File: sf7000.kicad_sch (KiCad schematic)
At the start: 114 parts

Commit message: labeled IC33
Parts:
- C1: value (none) -> 100u
- C10, C11, C18, C19, C20, C21, C22, C4, C43, C44, C5, C6, C7, C8, C9, C?: value (none) -> 100n
- C12, C13, C?: value (none) -> 33p
- C14: value (none) -> 470p
- C15, C16, C23: value (none) -> C
- C2, C38: value (none) -> 22p
- C34, C45: value (none) -> CP
- C35, C36: value (none) -> 10u
- C40, C41, C42: value (none) -> 220p
- CN1: value (none) -> Conn_01x03_Female
- CN2-A: value (none) -> Floppy_34pin
- CN2-B: value (none) -> Floppy_26pin
- CN3, CN?: value (none) -> Conn_02x17_Odd_Even
- CN4: value (none) -> Centronics 14 pin
- CN5: value (none) -> DB25_Female
- D1, D2, D7, D8: value (none) -> 1S1588
- D9: value (none) -> D_Zener
- DSW1: value (none) -> SW_DIP_x06
- IC10?, IC11?, IC12?, IC5, IC6, IC7, IC8, IC9?: value (none) -> MB8264
- IC13: value (none) -> M5L2764K
- IC14, IC21: value (none) -> 74LS00
- IC15: value (none) -> 74LS02
- IC16, IC17, IC37: value (none) -> 74LS04
- IC18: value (none) -> 74LS06
- IC19: value (none) -> 74LS07
- IC20: value (none) -> 74LS14
- IC22: value (none) -> 74LS139
- IC23, IC24, IC25: value (none) -> 74LS157
- IC26: value (none) -> 74LS32
- IC27, IC28: value (none) -> 74LS244
- IC3: value (none) -> uPD765A
- IC30: value (none) -> 74LS367
- IC33: renamed from U?; value (none) -> 8255A; footprint (none) -> Package_DIP:DIP-40_W15.24mm
- IC33: value (none) -> 8251
- IC34: value (none) -> SN75188
- IC35: value (none) -> SN75189
- IC36: value (none) -> 74LS293
- IC38: value (none) -> 4040
- IC4: value (none) -> SED9420C
- J?: value (none) -> JP_Overlay
- JP? (x2): value (none) -> SolderJumper_2_Open
- L?: value (none) -> L
- LED1: value (none) -> RD
- LED2: value (none) -> SD
- LED3: value (none) -> LED
- Q?: value (none) -> Q_PNP_ECB
- R1: value (none) -> 2K2
- R10: value (none) -> 1M
- R11, R14, R15, R4: value (none) -> 470
- R13: value (none) -> 220
- R16, R6: value (none) -> 10K
- R17: value (none) -> 18K
- R18, R19, RA1(1/8): value (none) -> 4k7
- R2, R7: value (none) -> 22K
- R20: value (none) -> 47K
- R3: value (none) -> 3K3
- R5: value (none) -> 4.7K
- R8: value (none) -> 150K
- R9: value (none) -> 560K
- RA1: value (none) -> K; footprint (none) -> Resistor_THT:R_Array_SIP9
- RA2: value (none) -> 1K; footprint (none) -> Resistor_THT:R_Array_SIP7
- RN?: value (none) -> R_Network08; footprint (none) -> Resistor_THT:R_Array_SIP9
- TR3: value (none) -> Q_NPN_ECB
- XAL2: value (none) -> 4.9152MHz
- XR1: value (none) -> 16Mhz

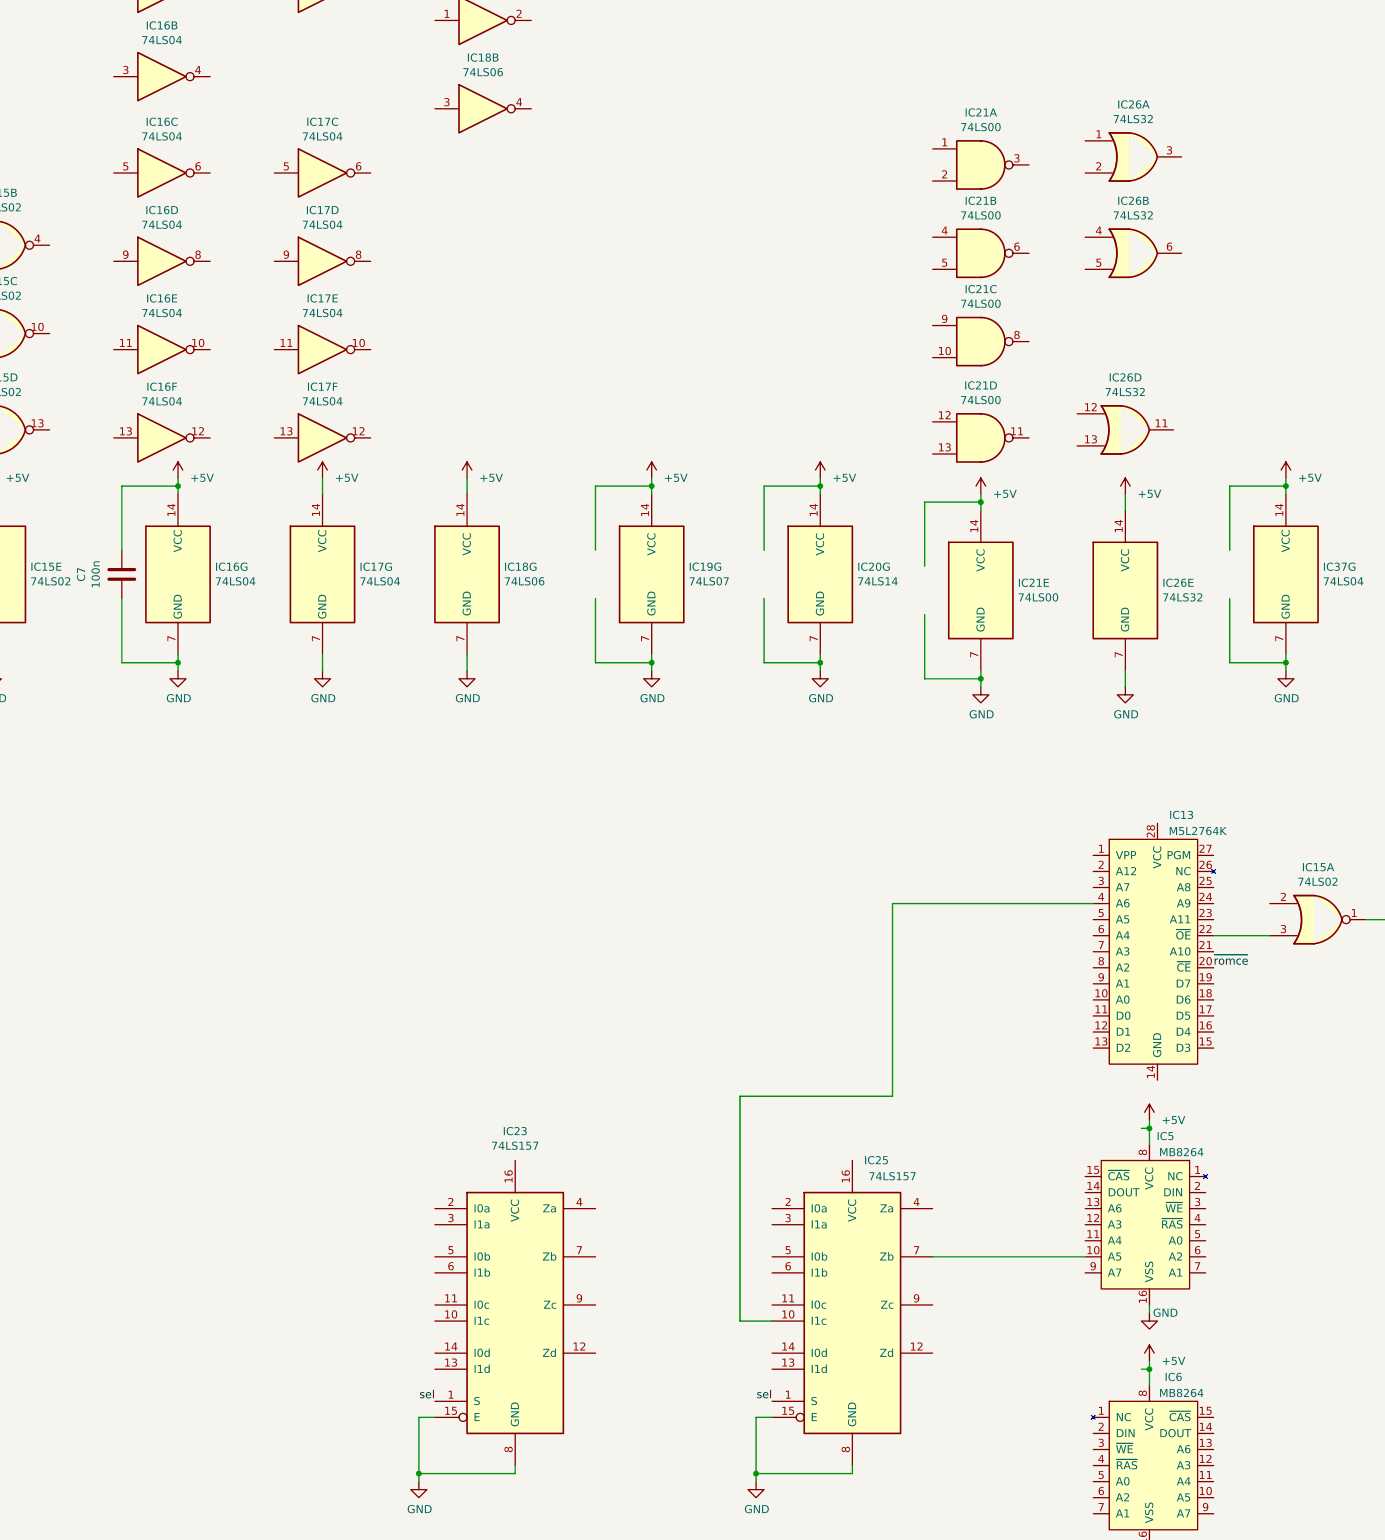
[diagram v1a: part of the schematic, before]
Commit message: IC25, info from andrea applied
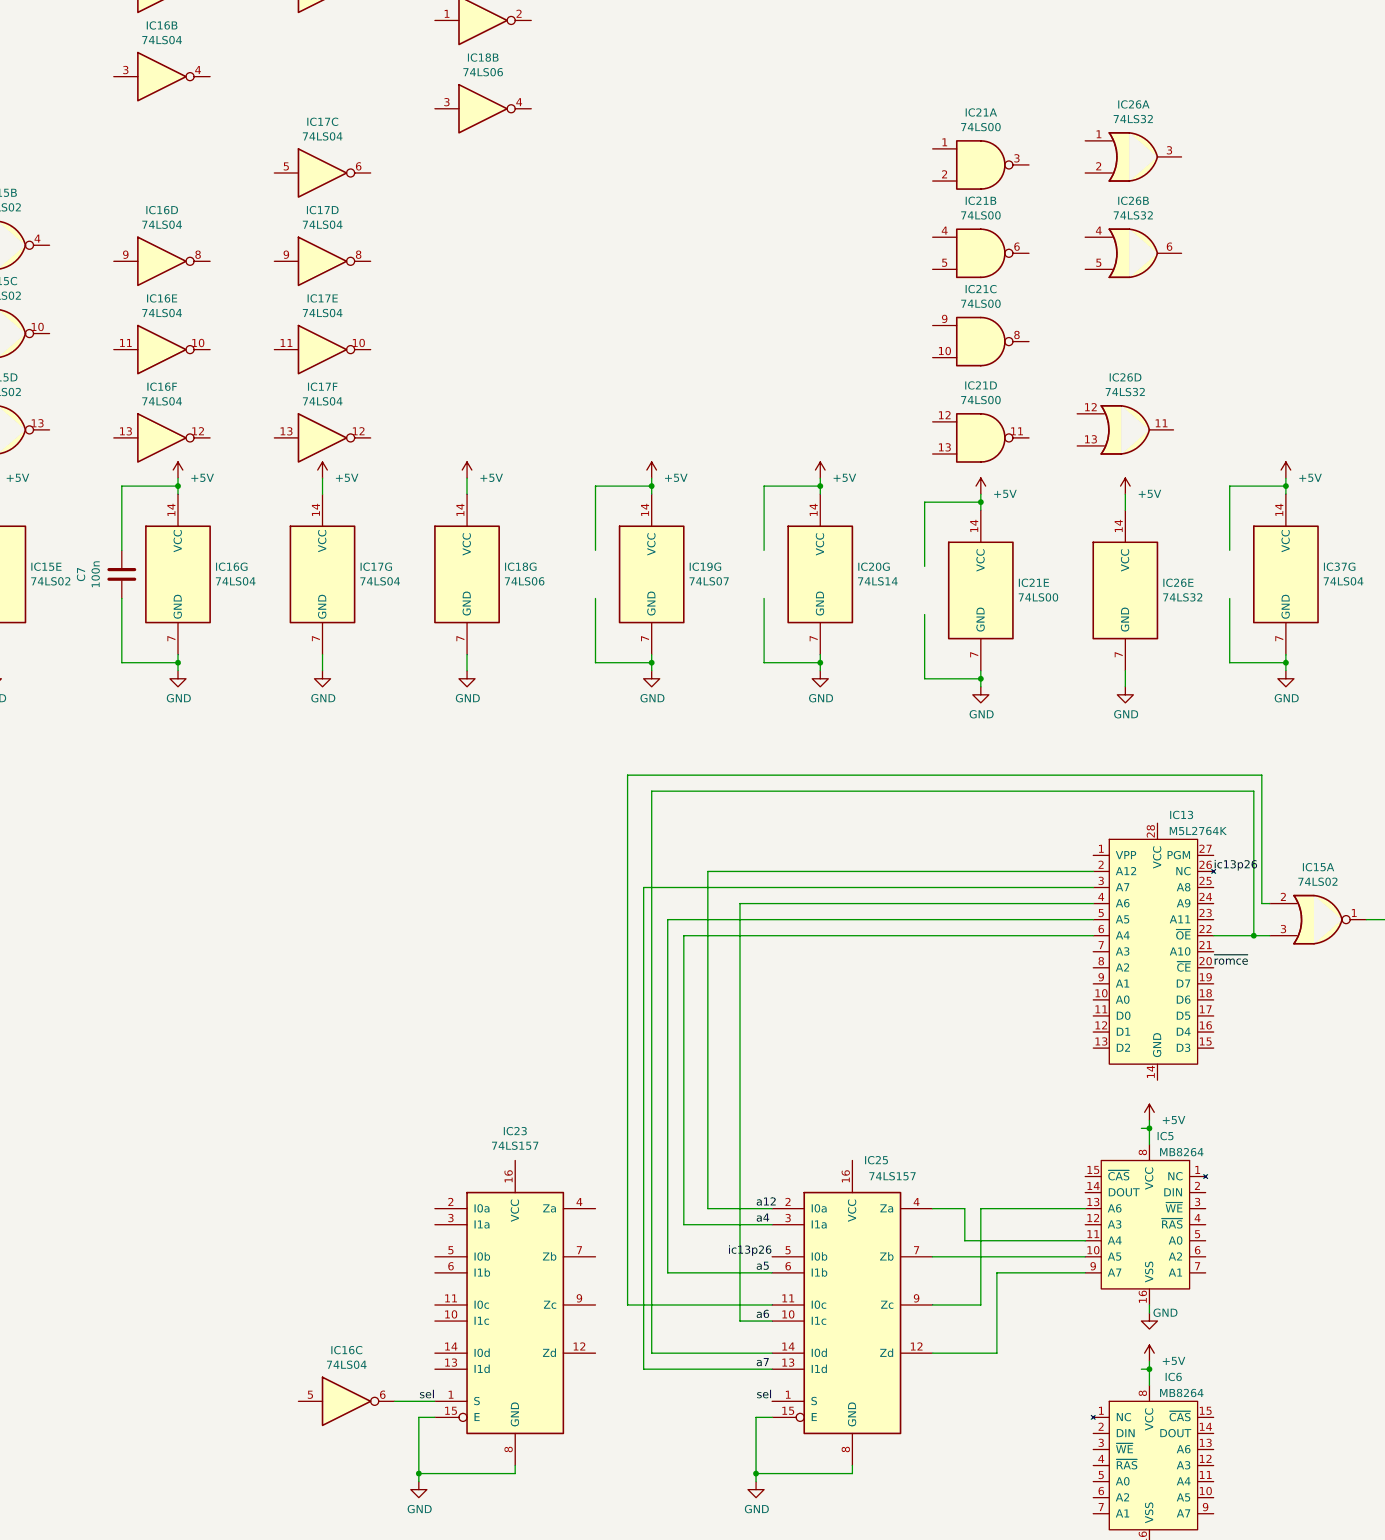
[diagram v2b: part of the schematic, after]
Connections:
- net a12: now also IC13.2 (A12), IC25.2 (I0a)
- net a4: now also IC13.6 (A4), IC25.3 (I1a)
- net a5: now also IC13.5 (A5), IC25.6 (I1b)
- net a6: now also IC13.4 (A6), IC25.10 (I1c)
- net a7: now also IC13.3 (A7), IC25.13 (I1d)
- net sel: now also IC16.6
- net at IC25.11 (I0c): now also IC15.2
- net at IC25.12 (Zd): now also IC5.9 (A7)
- net at IC25.14 (I0d): now also IC13.22 (~{OE}), IC15.3
- net at IC25.4 (Za): now also IC5.11 (A4)
- net ic13p26: now reaches IC25.5 (I0b)
- net ic13p26: now also IC13.26 (NC)
- net at IC25.9 (Zc): now also IC5.13 (A6)
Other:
- moved on the sheet: IC16C

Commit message: symbol for polarized cap
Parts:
- C1, C34, C35, C36, C45: symbol Device:CP -> Device:C_Polarized
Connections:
- net +5V: now also C1.1, C45.1
- net -12V: now also C35.2
- net GND: now also C1.2, C35.1, C36.2, C45.2
- net at C?.1, L?.2, TR3.2 (C): now also C34.1
- net at D1.1 (K), D2.2 (A): now also C34.2
- net at D7.2 (A), IC20.1, R6.2: now also C36.1
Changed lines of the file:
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@@
     (pin "7")
   )
-  (symbol (lib_id "Device:CP") (at 396.24 26.67 270) (unit 1)
+  (symbol (lib_id "Device:C_Polarized") (at 396.24 26.67 270) (unit 1)
     (in_bom yes) (on_board yes)
     (property "Reference" "C45" (id 0) (at 396.24 20.193 90))
@@
       (effects (font (size 1.27 1.27)) hide)
     )
+    (pin "1")
+    (pin "2")
   )
   (symbol (lib_id "power:GND") (at 391.16 26.67 270) (unit 1)
@@
     (pin "7")
   )
-  (symbol (lib_id "Device:CP") (at 97.79 152.4 90) (unit 1)
+  (symbol (lib_id "Device:C_Polarized") (at 97.79 152.4 90) (unit 1)
     (in_bom yes) (on_board yes)
     (property "Reference" "C34" (id 0) (at 97.79 156.21 90))
@@
       (effects (font (size 1.27 1.27)) hide)
     )
+    (pin "1")
+    (pin "2")
   )
   (symbol (lib_id "74xx:74LS00") (at 251.46 349.25 0) (unit 1)
@@
     (pin "7")
   )
-  (symbol (lib_id "Device:CP") (at 113.03 176.53 90) (unit 1)
+  (symbol (lib_id "Device:C_Polarized") (at 113.03 176.53 90) (unit 1)
     (in_bom yes) (on_board yes)
     (property "Reference" "C35" (id 0) (at 113.03 180.34 90))
@@
       (effects (font (size 1.27 1.27)) hide)
     )
+    (pin "1")
+    (pin "2")
   )
   (symbol (lib_id "Device:D_Zener") (at 113.03 168.91 0) (unit 1)
@@
     (pin "2")
   )
-  (symbol (lib_id "Device:CP") (at 33.02 209.55 0) (unit 1)
+  (symbol (lib_id "Device:C_Polarized") (at 33.02 209.55 0) (unit 1)
     (in_bom yes) (on_board yes)
     (property "Reference" "C36" (id 0) (at 26.543 209.55 90))
@@
       (effects (font (size 1.27 1.27)) hide)
     )
+    (pin "1")
+    (pin "2")
   )
   (symbol (lib_id "power:+5V") (at 33.02 193.04 0) (unit 1)
@@
     (pin "2")
   )
-  (symbol (lib_id "Device:CP") (at 45.72 148.59 0) (unit 1)
+  (symbol (lib_id "Device:C_Polarized") (at 45.72 148.59 0) (unit 1)
     (in_bom yes) (on_board yes)
     (property "Reference" "C1" (id 0) (at 39.243 148.59 90))
@@
       (effects (font (size 1.27 1.27)) hide)
     )
+    (pin "1")
+    (pin "2")
   )
   (symbol (lib_id "Connector:Conn_01x03_Female") (at 19.05 144.78 180) (unit 1)

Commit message: traced address decoding logic
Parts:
- removed C?: 33p, symbol Device:C
- removed RA1(1/8): 4k7, symbol Device:R
- added C24, C25, C26, C27, C37, C39: 100n, symbol Device:C
- added C_back1: 390p, symbol Device:C
- C1: value 100u -> 100uF 16v
- C15: value C -> 1nF
- RA1: value K -> 4K7
- gave numbers to parts that had none: 12
- renumbered CN2-A to CN2-A1, CN2-B to CN2-B1, IC33 to IC2
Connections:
- net 8355CS is gone; now on net 8255CS: IC22.5 (O1)
- net ic13p26 is gone; now on net a13: IC13.26 (NC), IC25.5 (I0b)
- net idcint is gone; now on net fdcint: IC4.5 (DRQ)
- net in_use is gone; now on an unnamed net: IC19.9
- net mot_on is gone; now on an unnamed net: IC19.13
- net ready is gone; now on net PPI_Ready: JP2.2 (B)
- net rstct is gone; now on net RESET: IC26.10
- net +5V: now also C10.2, C15.2, C18.2, C19.2, C20.2, C21.2, C22.2, C5.2, IC13.1 (VPP), IC13.27 (PGM), IC13.28 (VCC), IC23.16 (VCC), IC24.16 (VCC), IC25.16 (VCC), IC28.20 (VCC), R18.2, R19.2, RA1.1 (R1.1), C24.2, C25.2, C26.2, C27.2, C37.2, C39.2, C_back1.1; no longer C1.1
- net GND: now also C10.1, C15.1, C18.1, C19.1, C20.1, C21.1, C22.1, C5.1, IC13.14 (GND), IC33.4 (GND), R1.1, C24.1, C25.1, C26.1, C27.1, C37.1, C39.1; no longer C1.2
- net a0: now also IC13.10 (A0), IC2.9 (A0), IC23.3 (I1a), IC33.12 (C/D)
- net a1: now also IC13.9 (A1), IC2.8 (A1), IC23.6 (I1b)
- net a10: now also IC13.21 (A10), IC23.11 (I0c)
- net a11: now also IC13.23 (A11), IC23.14 (I0d)
- net a14: now also IC15.2, IC25.11 (I0c)
- net a15: now also IC15.3, IC25.14 (I0d)
- net a2: now also IC13.8 (A2), IC23.10 (I1c)
- net a3: now also IC13.7 (A3), IC23.13 (I1d)
- net a8: now also IC13.25 (A8), IC23.2 (I0a)
- net a9: now also IC13.24 (A9), IC23.5 (I0b)
- net d0: now also IC13.11 (D0), IC5.14 (DOUT), IC5.2 (DIN)
- net d1: now also IC13.12 (D1), IC6.14 (DOUT), IC6.2 (DIN)
- net d2: now also IC13.13 (D2), IC7.2 (DIN)
- net d3: now also IC13.15 (D3), IC8.14 (DOUT), IC8.2 (DIN)
- net d4: now also IC13.16 (D4), IC9.2 (DIN)
- net d5: now also IC10.2 (DIN), IC13.17 (D5)
- net d6: now also IC11.2 (DIN), IC13.18 (D6)
- net d7: now also IC12.2 (DIN), IC13.19 (D7)
- net fdcint: now also IC2.4 (PA0)
- net index: now also CN2-A1.8 (~{INDEX}), CN2-B1.2 (INDEX), IC20.13, RA2.2 (R1.2); no longer IC20.12, IC3.17 (IDX)
- net pbusy: now also IC2.3 (PA1), RA1.3 (R2.2)
- net pd0: now also IC2.18 (PB0)
- net pd1: now also IC2.19 (PB1)
- net pd2: now also IC2.20 (PB2)
- net pd3: now also IC2.21 (PB3)
- net pd4: now also IC2.22 (PB4)
- net pd5: now also IC2.23 (PB5)
- net pd6: now also IC2.24 (PB6)
- net pd7: now also IC2.25 (PB7)
- net reset55: now also IC2.35 (RESET)
- net tc: now also IC2.16 (PC2), RA1.7 (R6.2)
- net ~{ior}: now also IC21.13, R19.1
- net ~{iow}: now also IC21.1, R18.1
- net ~{memr}: now also IC21.12, IC26.5
- net ~{memw}: now also IC21.2, IC26.2
- net ~{mreq}: now also IC16.13
- net ~{pstb}: now also IC2.10 (PC7), RA1.4 (R3.2)
- net ~{romce}: now also IC14.1, IC17.4
- net at IC3.15 (~{DACK}): now also RA1.2 (R1.2)
- net A7_Ram: now reaches IC25.12 (Zd), IC5.9 (A7)
- net A7_Ram: now also IC10.9 (A7), IC11.9 (A7), IC12.9 (A7), IC6.9 (A7), IC7.9 (A7), IC8.9 (A7), IC9.9 (A7)
- net A4_Ram: now reaches IC25.4 (Za), IC5.11 (A4)
- net A4_Ram: now also IC10.11 (A4), IC11.11 (A4), IC12.11 (A4), IC6.11 (A4), IC7.11 (A4), IC8.11 (A4), IC9.11 (A4)
- net A5_Ram: now reaches IC25.7 (Zb), IC5.10 (A5)
- net A5_Ram: now also IC10.10 (A5), IC11.10 (A5), IC12.10 (A5), IC6.10 (A5), IC7.10 (A5), IC8.10 (A5), IC9.10 (A5)
- net A6_Ram: now reaches IC25.9 (Zc), IC5.13 (A6)
- net A6_Ram: now also IC10.13 (A6), IC11.13 (A6), IC12.13 (A6), IC6.13 (A6), IC7.13 (A6), IC8.13 (A6), IC9.13 (A6)
- net ~{ROMSEL}: now reaches IC2.11 (PC6)
- net ~{ROMSEL}: now also IC15.11, R1.2
- net PPI_Ready: now reaches IC2.12 (PC5)
- net at IC2.14 (PC0): now also RA1.9 (R8.2)
- net at IC2.15 (PC1): now also RA1.8 (R7.2)
- net RESET: now reaches IC2.17 (PC3)
- net RESET: now also RA1.6 (R5.2)
- net ~{PPI_WR}: now reaches IC2.36 (~{WR})
- net ~{PPI_WR}: now also IC21.6
- net ~{PPI_RD}: now reaches IC2.5 (~{RD})
- net ~{PPI_RD}: now also IC21.8
- net 8255CS: now reaches IC2.6 (~{CS})
- net at IC14.2: now also IC15.13, IC16.9
- net at IC14.3: now also IC14.4
- net A3_Ram: now reaches IC5.12 (A3)
- net A3_Ram: now also IC10.12 (A3), IC11.12 (A3), IC12.12 (A3), IC23.12 (Zd), IC6.12 (A3), IC7.12 (A3), IC8.12 (A3), IC9.12 (A3)
- net ~{CAS}: now reaches IC5.15 (~{CAS})
- net ~{CAS}: now also IC10.15 (~{CAS}), IC11.15 (~{CAS}), IC12.15 (~{CAS}), IC17.2, IC6.15 (~{CAS}), IC7.15 (~{CAS}), IC8.15 (~{CAS}), IC9.15 (~{CAS})
- net WE_Ram: now reaches IC5.3 (~{WE})
- net WE_Ram: now also IC10.3 (~{WE}), IC11.3 (~{WE}), IC12.3 (~{WE}), IC14.13, IC26.3, IC6.3 (~{WE}), IC7.3 (~{WE}), IC8.3 (~{WE}), IC9.3 (~{WE})
- net ~{RAS}: now reaches IC5.4 (~{RAS})
- net ~{RAS}: now also IC10.4 (~{RAS}), IC11.4 (~{RAS}), IC12.4 (~{RAS}), IC16.10, IC21.10, IC21.5, IC26.1, IC26.4, IC6.4 (~{RAS}), IC7.4 (~{RAS}), IC8.4 (~{RAS}), IC9.4 (~{RAS}), C_back1.2
- net A0_Ram: now reaches IC5.5 (A0)
- net A0_Ram: now also IC10.5 (A0), IC11.5 (A0), IC12.5 (A0), IC23.4 (Za), IC6.5 (A0), IC7.5 (A0), IC8.5 (A0), IC9.5 (A0)
- net A2_Ram: now reaches IC5.6 (A2)
- net A2_Ram: now also IC10.7 (A1), IC11.7 (A1), IC12.7 (A1), IC23.9 (Zc), IC6.7 (A1), IC7.7 (A1), IC8.7 (A1), IC9.7 (A1)
- net A1_Ram: now reaches IC5.7 (A1)
- net A1_Ram: now also IC10.6 (A2), IC11.6 (A2), IC12.6 (A2), IC23.7 (Zb), IC6.6 (A2), IC7.6 (A2), IC8.6 (A2), IC9.6 (A2)
- net at IC14.5: now also IC16.4, IC16.5
- net at IC14.6: now also IC17.13
- net at IC14.11: now also IC16.1
- net at IC14.12: now also IC15.12, IC26.6
- net IN_USE: now reaches CN2-A1.4 (IN_USE), IC19.8
- net at Q1.3 (B), R20.2: now also C1.2
- net at IC17.1: now also IC17.8
- net at IC17.9: now also IC17.10
- net ~{READY}: now reaches CN2-A1.34 (~{READY}), IC20.3, RA2.5 (R4.2)
- net ~{READY}: now also CN2-B1.26 (NC)
- net at IC17.11: now also IC17.12
- net at C34.1, L1.2, TR3.2 (C): now also C1.1
- net at IC16.2: now also IC16.3
- net ~{romOE}: now reaches IC16.8
- net ~{romOE}: now also IC13.22 (~{OE})
- net at IC16.11: now also IC16.12
- net at IC21.3: now also IC21.4
- net at IC21.9: now also IC21.11
- net 8251SS renamed 8251CS
- net motor_on renamed MOTOR_ON
- net sel renamed rcsel
- new net: IC20.12, IC3.17 (IDX)
- no-connect marks 30 -> 62
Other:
- note added: "Decoupling"
- note added: "Used by the serial"
- note removed: "???"
- note removed: "Undocumented"
- moved on the sheet: C10, C11, C12, C13, C14, C15, C16, C18, C19, C2, C20, C21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
